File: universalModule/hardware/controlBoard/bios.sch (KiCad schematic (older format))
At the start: 25 parts, among them J3 USB_ALT, J8 BIOS_SWD, P1 USB_C_Plug_USB2.0, U9 STM32F030C8Tx

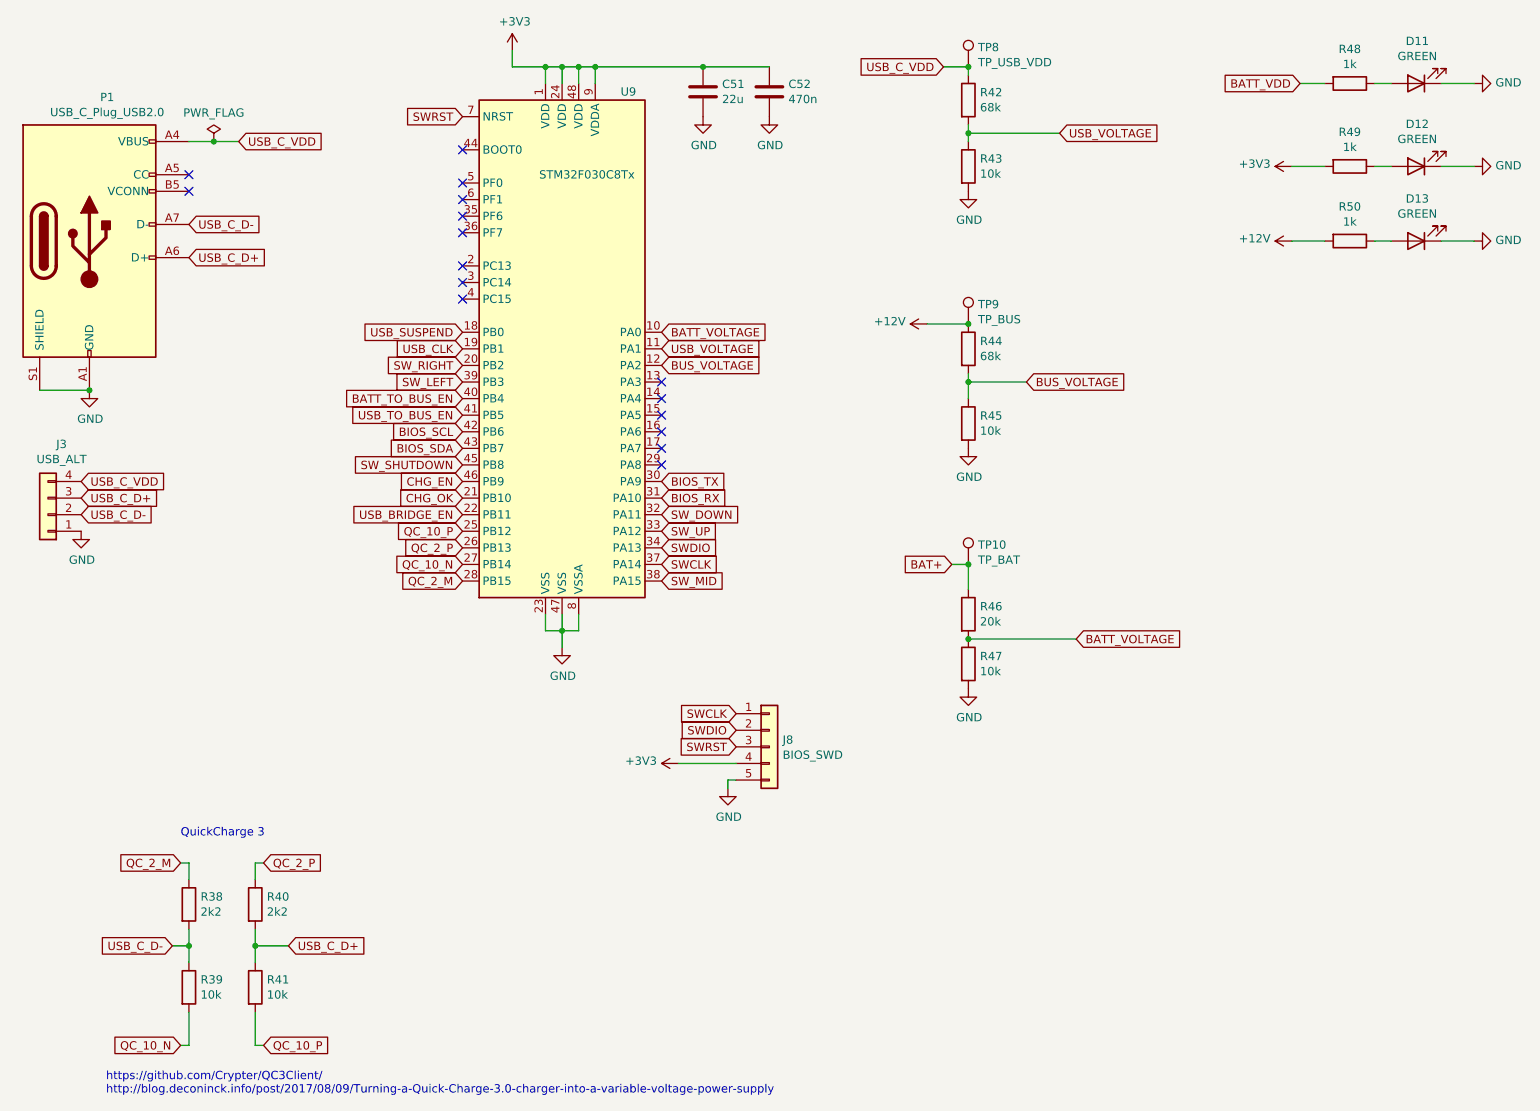
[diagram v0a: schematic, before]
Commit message: universalModule: Route the control boards
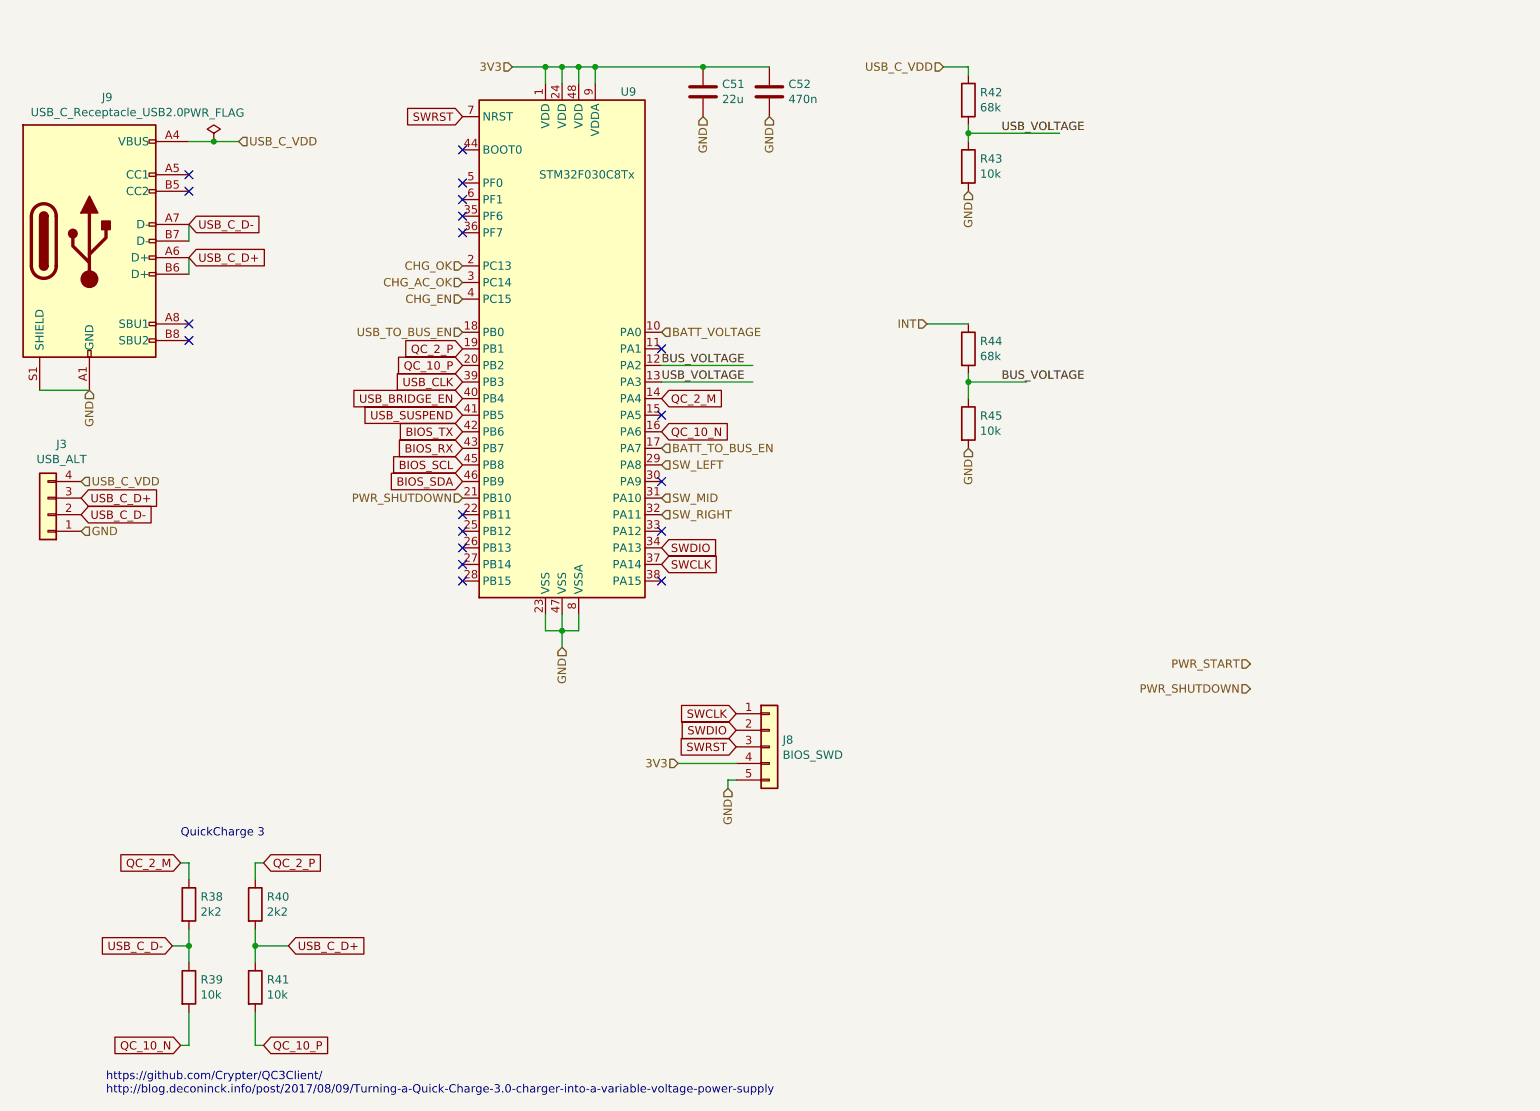
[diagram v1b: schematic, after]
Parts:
- removed D11, D12, D13: GREEN, LED_SMD:LED_0603_1608Metric, symbol Device:LED
- removed P1: USB_C_Plug_USB2.0, rofi:USB_C_Female-6Pin, symbol Connector:USB_C_Plug_USB2.0
- removed R46: 20k, Resistor_SMD:R_0402_1005Metric, symbol Device:R
- removed R47: 10k, Resistor_SMD:R_0402_1005Metric, symbol Device:R
- removed R48, R49, R50: 1k, Resistor_SMD:R_0402_1005Metric, symbol Device:R
- removed TP10: TP_BAT, TestPoint:TestPoint_Pad_D2.0mm, symbol Connector:TestPoint
- removed TP8: TP_USB_VDD, TestPoint:TestPoint_Pad_D2.0mm, symbol Connector:TestPoint
- removed TP9: TP_BUS, TestPoint:TestPoint_Pad_D2.0mm, symbol Connector:TestPoint
- added J9: USB_C_Receptacle_USB2.0, rofi:USB_C_Female-16Pin-HPJF, symbol Connector:USB_C_Receptacle_USB2.0
- J8: footprint Connector_PinHeader_2.54mm:PinHeader_1x05_P2.54mm_Vertical -> Connector_PinHeader_2.54mm:PinHeader_2x03_P2.54mm_Vertical
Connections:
- net labels added: 3V3, CHG_AC_OK, INT, PWR_SHUTDOWN, PWR_START
- net labels removed: +12V, +3V3, BAT+, BATT_VDD, SW_DOWN, SW_SHUTDOWN, SW_UP
- wire segments 58 -> 49
- no-connect marks 16 -> 19

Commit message: UniversalModule: Start version 2
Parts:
- removed J3: USB_ALT, Connector_PinHeader_2.54mm:PinHeader_1x04_P2.54mm_Vertical, symbol Connector_Generic:Conn_01x04
- removed J8: BIOS_SWD, Connector_PinHeader_2.54mm:PinHeader_2x03_P2.54mm_Vertical, symbol Connector_Generic:Conn_01x05
- removed J9: USB_C_Receptacle_USB2.0, rofi:USB_C_Female-16Pin-HPJF, symbol Connector:USB_C_Receptacle_USB2.0
- removed R38, R40: 2k2, Resistor_SMD:R_0402_1005Metric, symbol Device:R
- removed R39, R41, R43, R45: 10k, Resistor_SMD:R_0402_1005Metric, symbol Device:R
- removed R42, R44: 68k, Resistor_SMD:R_0402_1005Metric, symbol Device:R
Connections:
- net labels removed: INT, PWR_START, USB_C_D+, USB_C_D-, USB_C_VDD
- wire segments 49 -> 18
- no-connect marks 19 -> 15
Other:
- note removed: "QuickCharge 3"
- note removed: "https://github.com/Crypter/QC3Client/\nhttp://blog.deconinck.info/post/2017/08/09/Turning-a-Quick-Charge-3.0-charger-into-a-variable-voltage-power-supply"
